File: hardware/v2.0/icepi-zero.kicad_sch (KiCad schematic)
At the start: 29 parts, among them J1 Conn_02x20_Counter_Clockwise, SW1 SW_Push, SW2 SW_Push, U1 ECP5U-25F-CABGA256, Y1 SG-8018CG 50.000000MHz

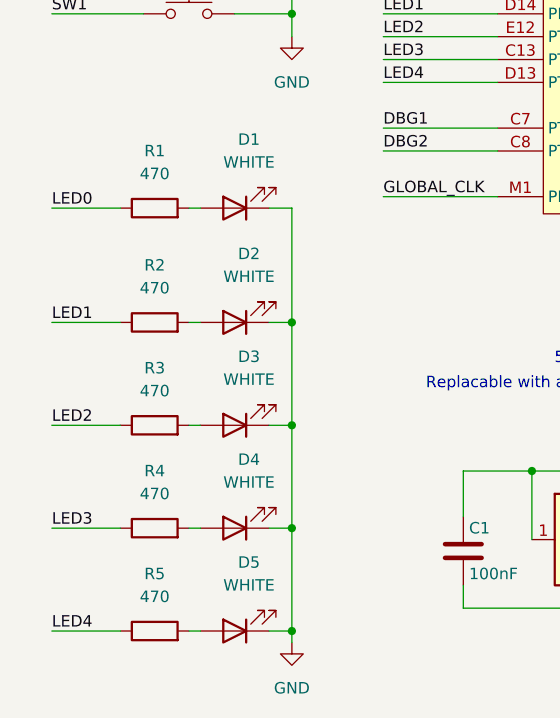
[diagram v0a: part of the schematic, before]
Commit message: LDOs dividers update
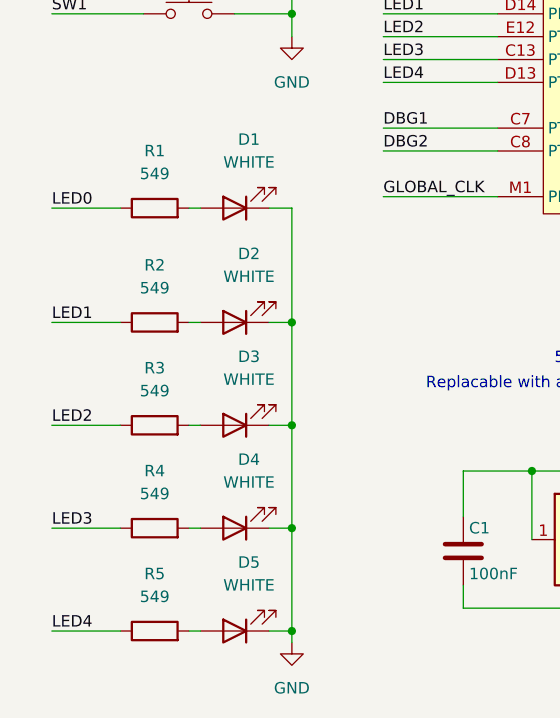
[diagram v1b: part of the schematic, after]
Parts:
- R1, R2, R3, R4, R5: value 470 -> 549; LCSC Link https://lcsc.com/product-detail/Chip-Resistor-Surface-Mount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 -> https://www.lcsc.com/product-detail/C474081.html; LCSC Part # C25117 -> C474081; Manufactuer Part Number 0402WGF4700TCE -> 0402WGF5490TCE
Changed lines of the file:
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@@
 			)
 		)
-		(property "Value" "470"
+		(property "Value" "549"
 			(at 33.02 157.48 90)
 			(effects
@@
 			)
 		)
-		(property "LCSC Part #" "C25117"
+		(property "LCSC Part #" "C474081"
 			(at 33.02 161.29 0)
 			(effects
@@
 			)
 		)
-		(property "LCSC Link" "https://lcsc.com/product-detail/Chip-Resistor-Surface-Mount_UNI-ROYAL-0402WGF4700TCE_C25117.html"
+		(property "LCSC Link" "https://www.lcsc.com/product-detail/C474081.html"
 			(at 33.02 161.29 90)
 			(effects
@@
 			)
 		)
-		(property "Manufactuer Part Number" "0402WGF4700TCE"
+		(property "Manufactuer Part Number" "0402WGF5490TCE"
 			(at 33.02 161.29 90)
 			(effects
@@
 			)
 		)
-		(property "Value" "470"
+		(property "Value" "549"
 			(at 33.02 180.34 90)
 			(effects
@@
 			)
 		)
-		(property "LCSC Part #" "C25117"
+		(property "LCSC Part #" "C474081"
 			(at 33.02 184.15 0)
 			(effects
@@
 			)
 		)
-		(property "LCSC Link" "https://lcsc.com/product-detail/Chip-Resistor-Surface-Mount_UNI-ROYAL-0402WGF4700TCE_C25117.html"
+		(property "LCSC Link" "https://www.lcsc.com/product-detail/C474081.html"
 			(at 33.02 184.15 90)
 			(effects
@@
 			)
 		)
-		(property "Manufactuer Part Number" "0402WGF4700TCE"
+		(property "Manufactuer Part Number" "0402WGF5490TCE"
 			(at 33.02 184.15 90)
 			(effects
@@
 			)
 		)
-		(property "Value" "470"
+		(property "Value" "549"
 			(at 33.02 133.35 90)
 			(effects
@@
 			)
 		)
-		(property "LCSC Part #" "C25117"
+		(property "LCSC Part #" "C474081"
 			(at 33.02 137.16 0)
 			(effects
@@
 			)
 		)
-		(property "LCSC Link" "https://lcsc.com/product-detail/Chip-Resistor-Surface-Mount_UNI-ROYAL-0402WGF4700TCE_C25117.html"
+		(property "LCSC Link" "https://www.lcsc.com/product-detail/C474081.html"
 			(at 33.02 137.16 90)
 			(effects
@@
 			)
 		)
-		(property "Manufactuer Part Number" "0402WGF4700TCE"
+		(property "Manufactuer Part Number" "0402WGF5490TCE"
 			(at 33.02 137.16 90)
 			(effects
@@
 			)
 		)
-		(property "Value" "470"
+		(property "Value" "549"
 			(at 33.02 146.05 90)
 			(effects
@@
 			)
 		)
-		(property "LCSC Part #" "C25117"
+		(property "LCSC Part #" "C474081"
 			(at 33.02 149.86 0)
 			(effects
@@
 			)
 		)
-		(property "LCSC Link" "https://lcsc.com/product-detail/Chip-Resistor-Surface-Mount_UNI-ROYAL-0402WGF4700TCE_C25117.html"
+		(property "LCSC Link" "https://www.lcsc.com/product-detail/C474081.html"
 			(at 33.02 149.86 90)
 			(effects
@@
 			)
 		)
-		(property "Manufactuer Part Number" "0402WGF4700TCE"
+		(property "Manufactuer Part Number" "0402WGF5490TCE"
 			(at 33.02 149.86 90)
 			(effects
@@
 			)
 		)
-		(property "Value" "470"
+		(property "Value" "549"
 			(at 33.02 168.91 90)
 			(effects
@@
 			)
 		)
-		(property "LCSC Part #" "C25117"
+		(property "LCSC Part #" "C474081"
 			(at 33.02 172.72 0)
 			(effects
@@
 			)
 		)
-		(property "LCSC Link" "https://lcsc.com/product-detail/Chip-Resistor-Surface-Mount_UNI-ROYAL-0402WGF4700TCE_C25117.html"
+		(property "LCSC Link" "https://www.lcsc.com/product-detail/C474081.html"
 			(at 33.02 172.72 90)
 			(effects
@@
 			)
 		)
-		(property "Manufactuer Part Number" "0402WGF4700TCE"
+		(property "Manufactuer Part Number" "0402WGF5490TCE"
 			(at 33.02 172.72 90)
 			(effects

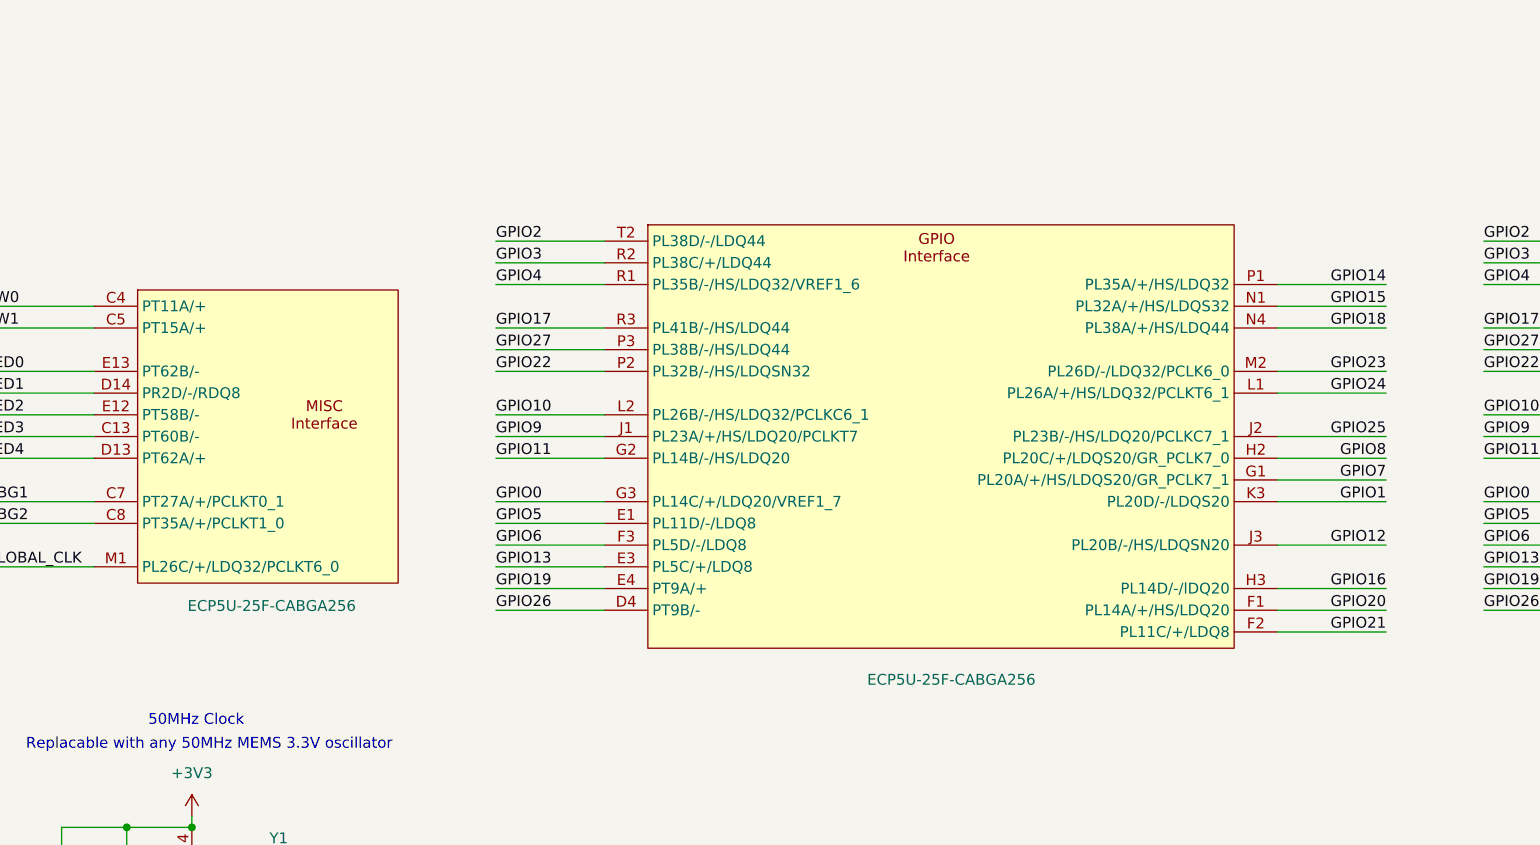
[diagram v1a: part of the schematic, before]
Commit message: ADC 6 diff lines
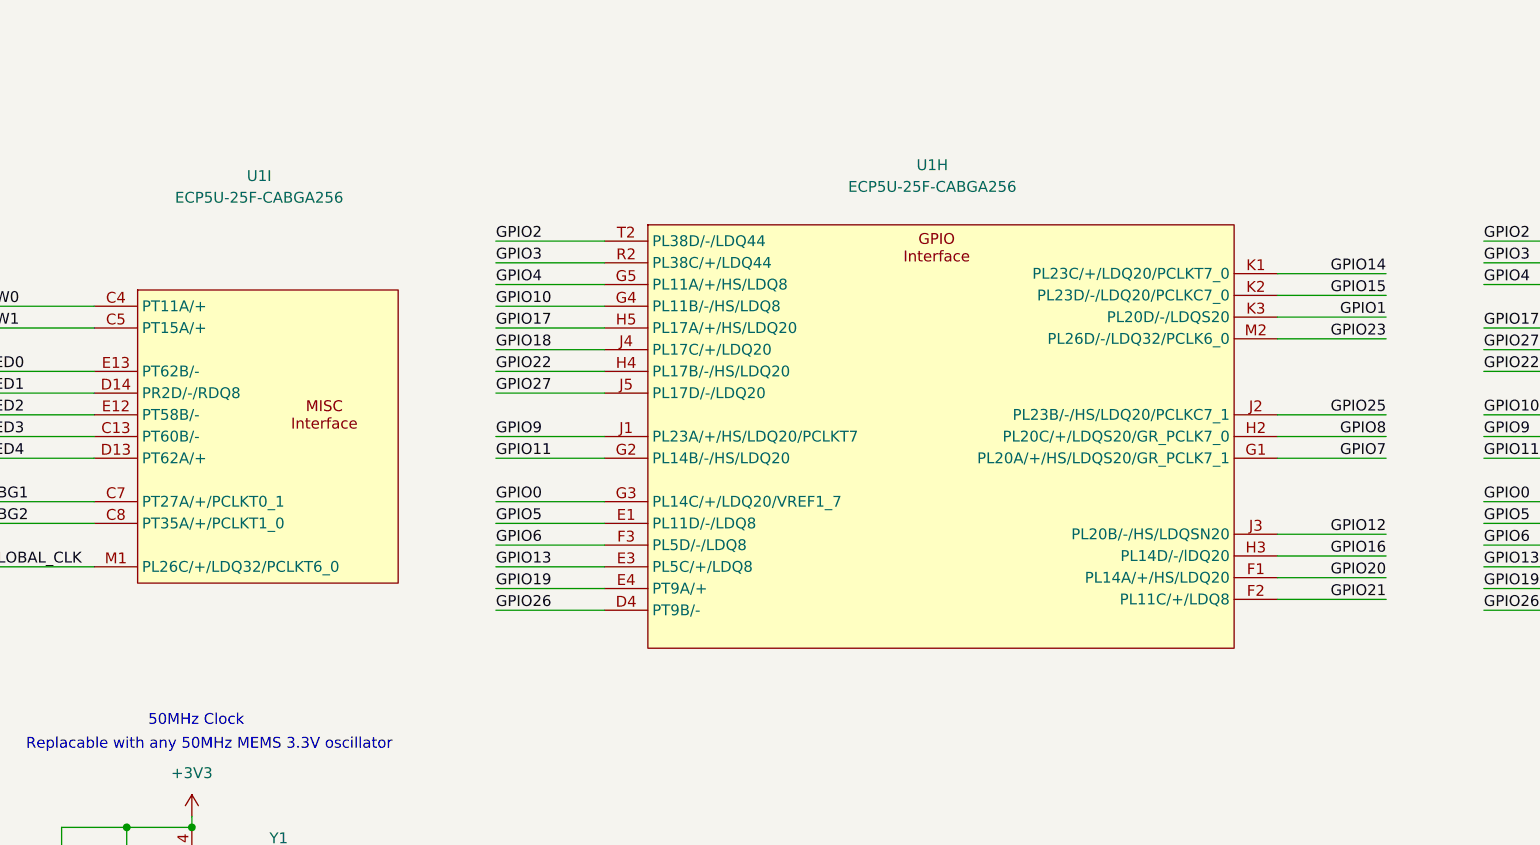
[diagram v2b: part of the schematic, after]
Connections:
- net GPIO10: now also U1.G4 (PL11B/-/HS/LDQ8); no longer U1.L2 (PL26B/-/HS/LDQ32/PCLKC6_1)
- net GPIO14: now also U1.K1 (PL23C/+/LDQ20/PCLKT7_0); no longer U1.P1 (PL35A/+/HS/LDQ32)
- net GPIO15: now also U1.K2 (PL23D/-/LDQ20/PCLKC7_0); no longer U1.N1 (PL32A/+/HS/LDQS32)
- net GPIO17: now also U1.H5 (PL17A/+/HS/LDQ20); no longer U1.R3 (PL41B/-/HS/LDQ44)
- net GPIO18: now also U1.J4 (PL17C/+/LDQ20); no longer U1.N4 (PL38A/+/HS/LDQ44)
- net GPIO22: now also U1.H4 (PL17B/-/HS/LDQ20); no longer U1.P2 (PL32B/-/HS/LDQSN32)
- net GPIO24: no longer U1.L1 (PL26A/+/HS/LDQ32/PCLKT6_1)
- net GPIO27: now also U1.J5 (PL17D/-/LDQ20); no longer U1.P3 (PL38B/-/HS/LDQ44)
- net GPIO4: now also U1.G5 (PL11A/+/HS/LDQ8); no longer U1.R1 (PL35B/-/HS/LDQ32/VREF1_6)

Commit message: ADC lines
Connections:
- net GPIO10: now also U1.M2 (PL26D/-/LDQ32/PCLK6_0); no longer U1.G4 (PL11B/-/HS/LDQ8)
- net GPIO14: now also U1.R4 (PL41C/+/LD44); no longer U1.K1 (PL23C/+/LDQ20/PCLKT7_0)
- net GPIO15: now also U1.M3 (PL32D/-/LDQ32); no longer U1.K2 (PL23D/-/LDQ20/PCLKC7_0)
- net GPIO18: now also U1.L3 (PL32C/+/LDQ32); no longer U1.J4 (PL17C/+/LDQ20)
- net GPIO24: now also U1.G4 (PL11B/-/HS/LDQ8)
- net GPIO4: now also U1.M6 (PL47A/+/HS/LDQ44); no longer U1.G5 (PL11A/+/HS/LDQ8)
- net GPIO17: no longer names the net of J1.11 (Pin_11)
- net GPIO17: no longer U1.H5 (PL17A/+/HS/LDQ20)
- net GPIO22: no longer names the net of J1.15 (Pin_15)
- net GPIO22: no longer U1.H4 (PL17B/-/HS/LDQ20)
- net GPIO23: no longer names the net of J1.16 (Pin_16)
- net GPIO23: no longer U1.M2 (PL26D/-/LDQ32/PCLK6_0)
- net GPIO27: no longer names the net of J1.13 (Pin_13)
- net GPIO27: no longer U1.J5 (PL17D/-/LDQ20)
- no-connect marks 0 -> 11
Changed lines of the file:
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@@
 		(color 0 0 0 0)
 	)
-	(wire
-		(pts
-			(xy 130.81 110.49) (xy 118.11 110.49)
-		)
-		(stroke
-			(width 0)
-			(type default)
-		)
+	(no_connect
+		(at 248.92 110.49)
+	)
+	(no_connect
+		(at 130.81 102.87)
+	)
+	(no_connect
+		(at 261.62 113.03)
+	)
+	(no_connect
+		(at 130.81 115.57)
+	)
+	(no_connect
+		(at 130.81 110.49)
+	)
+	(no_connect
+		(at 209.55 104.14)
+	)
+	(no_connect
+		(at 130.81 113.03)
+	)
+	(no_connect
+		(at 130.81 107.95)
+	)
+	(no_connect
+		(at 248.92 113.03)
+	)
+	(no_connect
+		(at 209.55 101.6)
+	)
+	(no_connect
+		(at 248.92 107.95)
 	)
 	(wire
@@
 	(wire
 		(pts
-			(xy 118.11 97.79) (xy 130.81 97.79)
+			(xy 209.55 111.76) (xy 222.25 111.76)
 		)
 		(stroke
@@
 	(wire
 		(pts
-			(xy 58.42 115.57) (xy 71.12 115.57)
+			(xy 118.11 97.79) (xy 130.81 97.79)
 		)
 		(stroke
@@
 	(wire
 		(pts
-			(xy 58.42 113.03) (xy 71.12 113.03)
+			(xy 58.42 115.57) (xy 71.12 115.57)
 		)
 		(stroke
@@
 	(wire
 		(pts
-			(xy 209.55 137.16) (xy 222.25 137.16)
+			(xy 58.42 113.03) (xy 71.12 113.03)
 		)
 		(stroke
@@
 	(wire
 		(pts
-			(xy 209.55 101.6) (xy 222.25 101.6)
+			(xy 209.55 137.16) (xy 222.25 137.16)
 		)
 		(stroke
@@
 	(wire
 		(pts
-			(xy 233.68 107.95) (xy 248.92 107.95)
-		)
-		(stroke
-			(width 0)
-			(type default)
-		)
-	)
-	(wire
-		(pts
 			(xy 233.68 97.79) (xy 248.92 97.79)
 		)
@@
 	(wire
 		(pts
-			(xy 261.62 102.87) (xy 276.86 102.87)
+			(xy 209.55 125.73) (xy 222.25 125.73)
 		)
 		(stroke
@@
 	(wire
 		(pts
-			(xy 261.62 113.03) (xy 276.86 113.03)
+			(xy 261.62 102.87) (xy 276.86 102.87)
 		)
 		(stroke
@@
 	(wire
 		(pts
-			(xy 233.68 110.49) (xy 248.92 110.49)
-		)
-		(stroke
-			(width 0)
-			(type default)
-		)
-	)
-	(wire
-		(pts
 			(xy 209.55 120.65) (xy 222.25 120.65)
 		)
@@
 	(wire
 		(pts
-			(xy 118.11 113.03) (xy 130.81 113.03)
-		)
-		(stroke
-			(width 0)
-			(type default)
-		)
-	)
-	(wire
-		(pts
 			(xy 48.26 137.16) (xy 48.26 149.86)
 		)
@@
 	(wire
 		(pts
-			(xy 118.11 102.87) (xy 130.81 102.87)
-		)
-		(stroke
-			(width 0)
-			(type default)
-		)
-	)
-	(wire
-		(pts
 			(xy 261.62 128.27) (xy 276.86 128.27)
 		)
@@
 	(wire
 		(pts
-			(xy 118.11 107.95) (xy 130.81 107.95)
-		)
-		(stroke
-			(width 0)
-			(type default)
-		)
-	)
-	(wire
-		(pts
 			(xy 233.68 130.81) (xy 248.92 130.81)
 		)
@@
 	(wire
 		(pts
-			(xy 261.62 107.95) (xy 276.86 107.95)
+			(xy 209.55 128.27) (xy 222.25 128.27)
 		)
 		(stroke
@@
 	(wire
 		(pts
-			(xy 233.68 113.03) (xy 248.92 113.03)
+			(xy 261.62 107.95) (xy 276.86 107.95)
 		)
 		(stroke
@@
 	(wire
 		(pts
-			(xy 118.11 115.57) (xy 130.81 115.57)
-		)
-		(stroke
-			(width 0)
-			(type default)
-		)
-	)
-	(wire
-		(pts
 			(xy 209.55 123.19) (xy 222.25 123.19)
 		)
@@
 	(wire
 		(pts
-			(xy 209.55 104.14) (xy 222.25 104.14)
-		)
-		(stroke
-			(width 0)
-			(type default)
-		)
-	)
-	(wire
-		(pts
 			(xy 233.68 128.27) (xy 248.92 128.27)
 		)
@@
 	(wire
 		(pts
+			(xy 209.55 114.3) (xy 222.25 114.3)
+		)
+		(stroke
+			(width 0)
+			(type default)
+		)
+	)
+	(wire
+		(pts
 			(xy 261.62 120.65) (xy 276.86 120.65)
 		)
@@
 		)
 	)
-	(label "GPIO14"
-		(at 222.25 101.6 180)
+	(label "GPIO24"
+		(at 125.73 105.41 180)
 		(effects
 			(font
@@
 		)
 	)
-	(label "GPIO27"
-		(at 233.68 110.49 0)
-		(effects
-			(font
-				(size 1.27 1.27)
-			)
-			(justify left bottom)
-		)
-	)
-	(label "GPIO23"
-		(at 276.86 113.03 180)
+	(label "GPIO18"
+		(at 222.25 114.3 180)
 		(effects
 			(font
@@
 		)
 	)
-	(label "GPIO17"
-		(at 118.11 107.95 0)
-		(effects
-			(font
-				(size 1.27 1.27)
-			)
-			(justify left bottom)
-		)
-	)
 	(label "GPIO16"
 		(at 276.86 138.43 180)
@@
 		)
 	)
-	(label "GPIO24"
-		(at 276.86 115.57 180)
+	(label "GPIO10"
+		(at 215.9 109.22 0)
 		(effects
 			(font
 				(size 1.27 1.27)
 			)
-			(justify right bottom)
+			(justify left bottom)
 		)
 	)
-	(label "GPIO20"
-		(at 222.25 137.16 180)
+	(label "GPIO24"
+		(at 276.86 115.57 180)
 		(effects
 			(font
@@
 		)
 	)
-	(label "GPIO22"
-		(at 233.68 113.03 0)
+	(label "GPIO20"
+		(at 222.25 137.16 180)
 		(effects
 			(font
 				(size 1.27 1.27)
 			)
-			(justify left bottom)
+			(justify right bottom)
 		)
 	)
@@
 		)
 	)
-	(label "GPIO15"
-		(at 222.25 104.14 180)
-		(effects
-			(font
-				(size 1.27 1.27)
-			)
-			(justify right bottom)
-		)
-	)
-	(label "GPIO17"
-		(at 233.68 107.95 0)
-		(effects
-			(font
-				(size 1.27 1.27)
-			)
-			(justify left bottom)
-		)
-	)
 	(label "GPIO1"
 		(at 276.86 128.27 180)
@@
 		)
 	)
-	(label "GPIO10"
-		(at 118.11 105.41 0)
+	(label "GPIO4"
+		(at 215.9 111.76 0)
 		(effects
 			(font
@@
 		)
 	)
-	(label "GPIO23"
-		(at 222.25 109.22 180)
-		(effects
-			(font
-				(size 1.27 1.27)
-			)
-			(justify right bottom)
-		)
-	)
 	(label "GPIO26"
 		(at 118.11 140.97 0)
@@
 		)
 	)
-	(label "GPIO13"
-		(at 233.68 135.89 0)
+	(label "GPIO14"
+		(at 222.25 125.73 180)
 		(effects
 			(font
 				(size 1.27 1.27)
 			)
-			(justify left bottom)
+			(justify right bottom)
 		)
 	)
-	(label "GPIO27"
-		(at 118.11 115.57 0)
+	(label "GPIO13"
+		(at 233.68 135.89 0)
 		(effects
 			(font
@@
 		)
 	)
-	(label "GPIO22"
-		(at 118.11 113.03 0)
-		(effects
-			(font
-				(size 1.27 1.27)
-			)
-			(justify left bottom)
-		)
-	)
-	(label "GPIO18"
-		(at 118.11 110.49 0)
-		(effects
-			(font
-				(size 1.27 1.27)
-			)
-			(justify left bottom)
-		)
-	)
 	(label "DBG1"
 		(at 144.78 184.15 90)
@@
 		)
 	)
-	(label "GPIO4"
-		(at 118.11 102.87 0)
+	(label "LED0"
+		(at 58.42 113.03 0)
 		(effects
 			(font
@@
 		)
 	)
-	(label "LED0"
-		(at 58.42 113.03 0)
+	(label "GPIO8"
+		(at 222.25 120.65 180)
 		(effects
 			(font
 				(size 1.27 1.27)
 			)
-			(justify left bottom)
+			(justify right bottom)
 		)
 	)
-	(label "GPIO8"
-		(at 222.25 120.65 180)
+	(label "GPIO15"
+		(at 222.25 128.27 180)
 		(effects
 			(font
@@
 		(on_board yes)
 		(dnp no)
-		(fields_autoplaced yes)
 		(property "Reference" "U1"
 			(at 169.164 88.9 0)
@@
 					(reference "U1")
 					(unit 9)
-				)
-				(path "/f88da08e-cf42-4d03-a08f-3f602fe6658d/b5a9aa02-311b-4a9a-a7d4-646f15cdd9c2"
-					(reference "U1")
-					(unit 9)

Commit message: ADC CLKOUT±
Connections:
- net GPIO4: no longer U1.M6 (PL47A/+/HS/LDQ44)
- no-connect marks 11 -> 4
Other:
- company: Chengyin Yao (cheyao), Vadym Vikulin -> Vadym Vikulin, Chengyin Yao (cheyao)
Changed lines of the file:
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@@
 	(title_block
 		(title "Icepi Zero")
-		(date "2026-01-05")
-		(rev "v2.0")
-		(company "Chengyin Yao (cheyao), Vadym Vikulin")
-		(comment 1 "https://github.com/cheyao/icepi-zero")
+		(date "2026-01-17")
+		(rev "v2.1")
+		(company "Vadym Vikulin, Chengyin Yao (cheyao)")
+		(comment 1 "https://github.com/vikulin/icepi-zero")
 		(comment 2 "License: Solderpad")
 		(comment 9 "OSHWA FR000026")
@@
 	)
 	(no_connect
-		(at 130.81 102.87)
-	)
-	(no_connect
 		(at 261.62 113.03)
 	)
 	(no_connect
-		(at 130.81 115.57)
-	)
-	(no_connect
-		(at 130.81 110.49)
-	)
-	(no_connect
-		(at 209.55 104.14)
-	)
-	(no_connect
-		(at 130.81 113.03)
-	)
-	(no_connect
-		(at 130.81 107.95)
-	)
-	(no_connect
 		(at 248.92 113.03)
 	)
 	(no_connect
-		(at 209.55 101.6)
-	)
-	(no_connect
 		(at 248.92 107.95)
 	)
@@
 	(wire
 		(pts
-			(xy 209.55 111.76) (xy 222.25 111.76)
-		)
-		(stroke
-			(width 0)
-			(type default)
-		)
-	)
-	(wire
-		(pts
 			(xy 118.11 97.79) (xy 130.81 97.79)
 		)
@@
 		)
 	)
-	(label "GPIO4"
-		(at 215.9 111.76 0)
-		(effects
-			(font
-				(size 1.27 1.27)
-			)
-			(justify left bottom)
-		)
-	)
 	(label "GPIO26"
 		(at 118.11 140.97 0)
@@
 		(pin "G13"
 		)
+		(pin "N6"
+		)
 		(instances
 			(project ""
@@
 		(pin "F8"
 		)
+		(pin "N6"
+		)
 		(instances

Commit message: ADC power
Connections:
- net GPIO4: no longer names the net of J1.7 (Pin_7)
- no-connect marks 4 -> 5
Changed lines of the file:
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@@
+	)
+	(no_connect
+		(at 248.92 102.87)
 	)
 	(no_connect
 		(at 248.92 107.95)
-	)
-	(wire
-		(pts
-			(xy 233.68 102.87) (xy 248.92 102.87)
-		)
-		(stroke
-			(width 0)
-			(type default)
-		)
 	)
 	(wire
@@
 		)
 	)
-	(label "GPIO4"
-		(at 233.68 102.87 0)
-		(effects
-			(font
-				(size 1.27 1.27)
-			)
-			(justify left bottom)
-		)
-	)
